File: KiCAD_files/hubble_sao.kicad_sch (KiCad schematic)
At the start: 41 parts, among them J1 Conn_02x03_Counter_Clockwise, J2 Conn_02x03_Odd_Even, Q1 DMP3099L-7, SW1 SW_Push_Shielded, U1 VEML3328, U2 LSM6DSO, U3 ATmega328PB-A, U4 TLV9062xD, U5 TLV9062xD

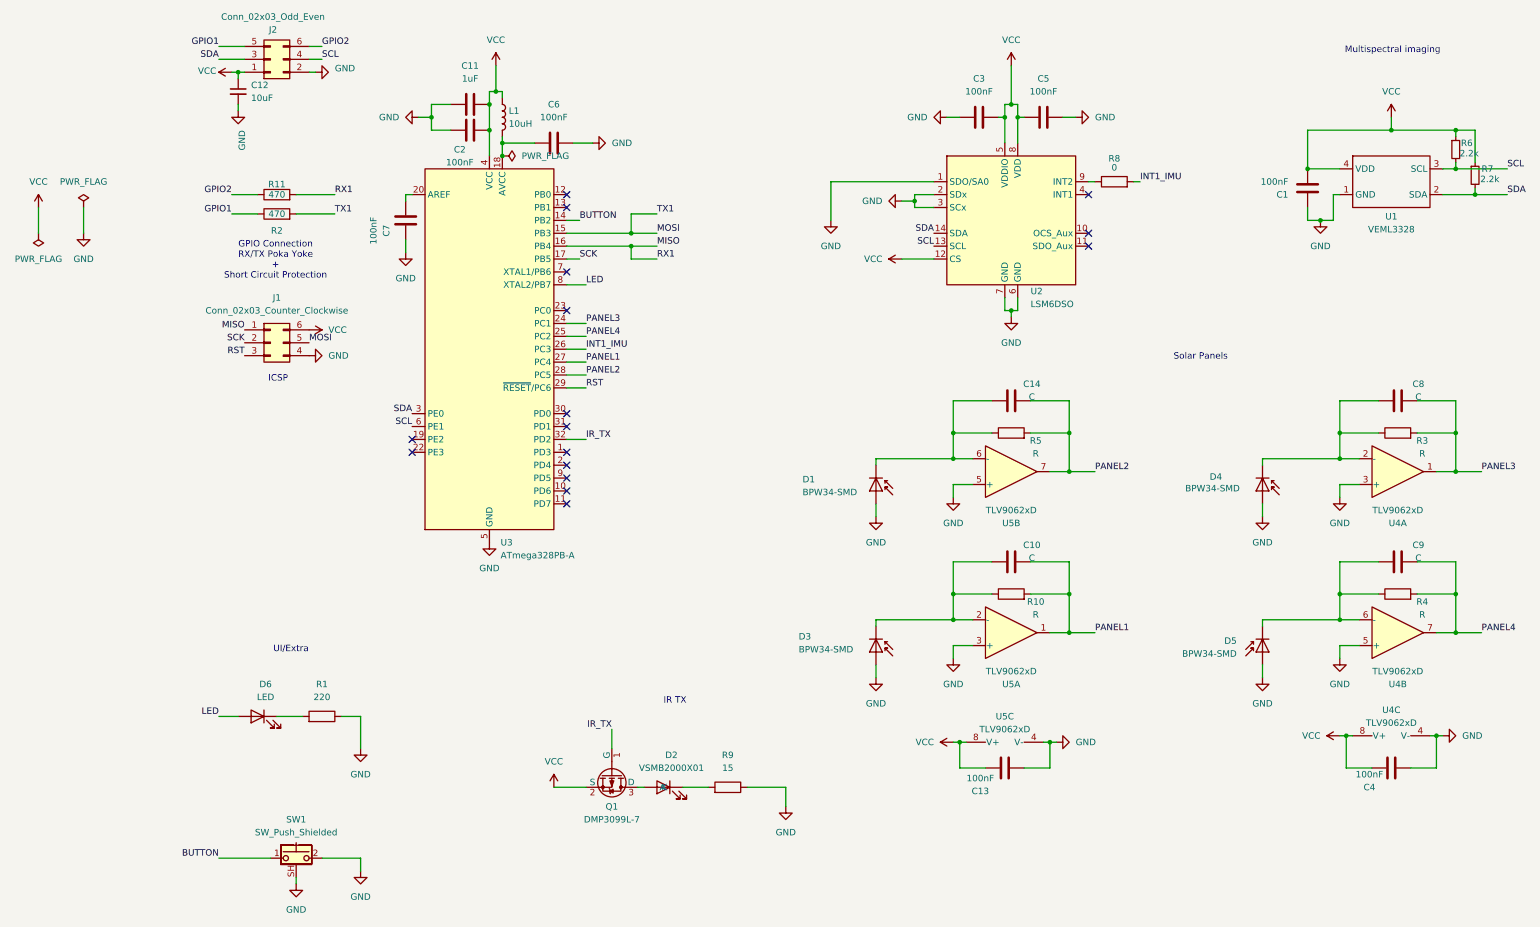
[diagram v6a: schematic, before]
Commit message: Modified RESET circuitry
- Added a switch to multiplex RESET and SCL on the pin header
- Added short-circuit protection on the RESET pin
- Added missing pullup resistor on the RESET pin. Before, RESET
was left floating. No problem was noticed on the prototype.
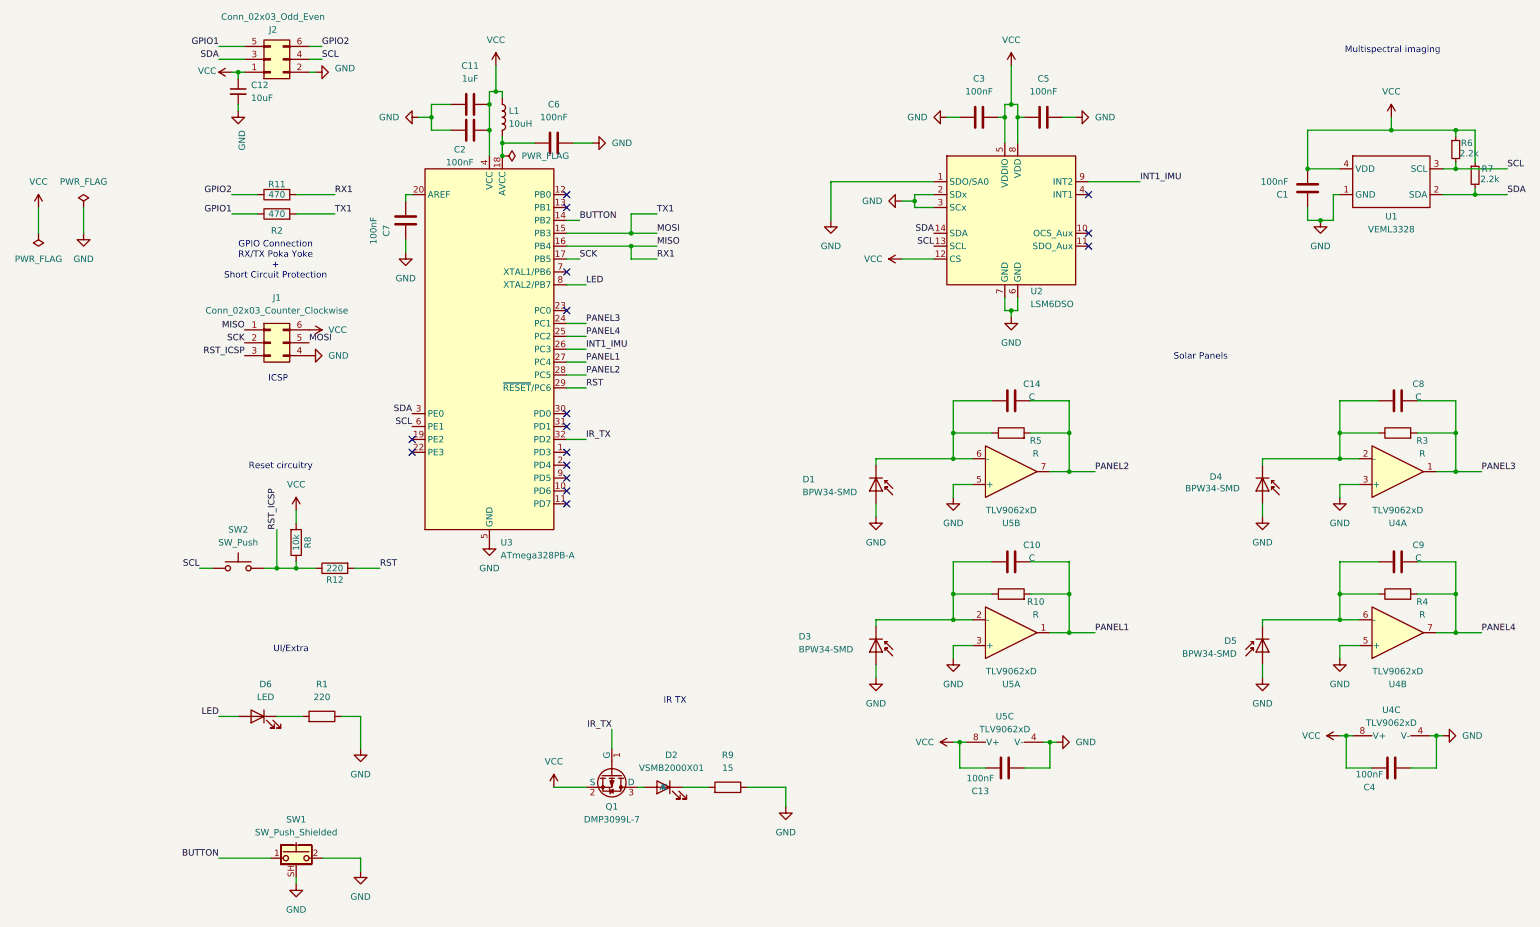
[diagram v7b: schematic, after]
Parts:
- added R12: 220, Resistor_SMD:R_0805_2012Metric_Pad1.20x1.40mm_HandSolder, symbol Device:R
- added SW2: SW_Push, Button_Switch_SMD:SW_SPST_B3U-1000P, symbol Switch:SW_Push
- R8: value 0 -> 10k
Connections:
- net INT1_IMU: now also U2.9 (INT2); no longer R8.2
- net RST: now also R12.2; no longer J1.3 (Pin_3)
- net SCL: now also SW2.1
- net VCC: now also R8.2
- net RST_ICSP: now reaches R8.1
- net RST_ICSP: now also J1.3 (Pin_3), R12.1, SW2.2; no longer U2.9 (INT2)
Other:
- note added: "Reset circuitry"

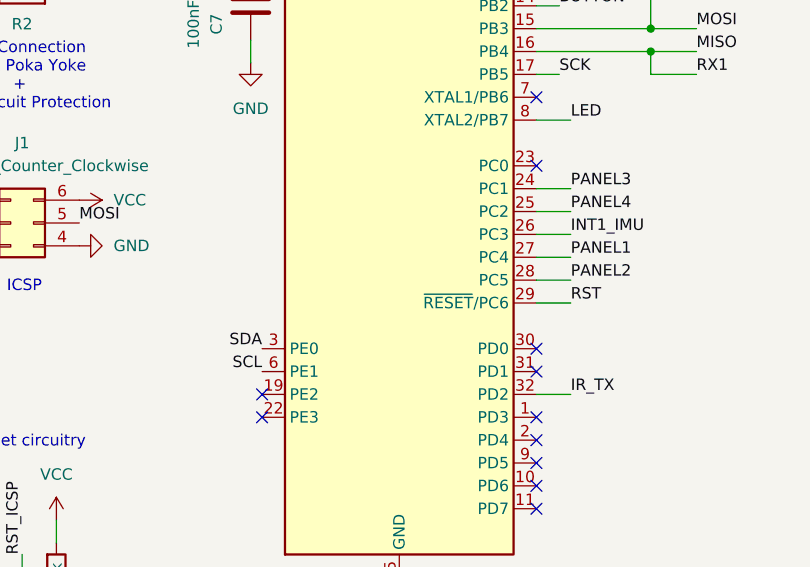
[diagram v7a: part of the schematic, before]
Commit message: Moved Panel3 to 19/PE2/ADC6/ICP3
This should enable the use of the Input Capture Pin 3.
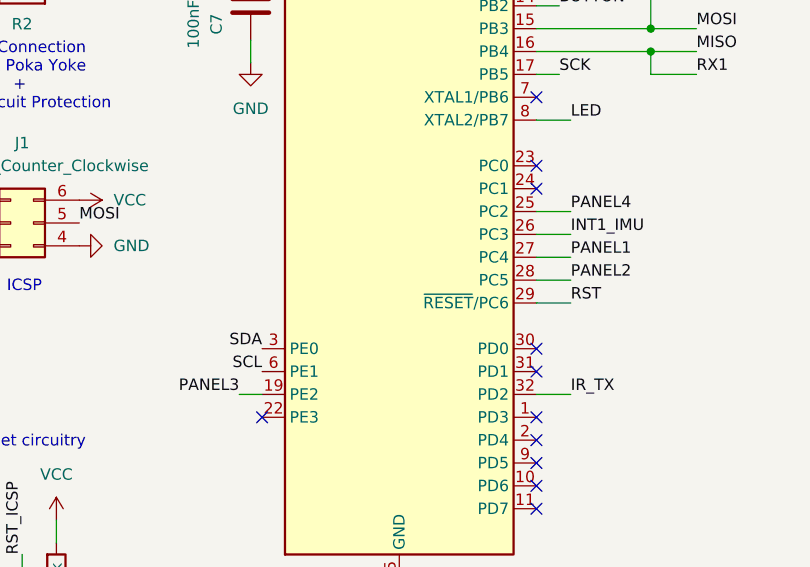
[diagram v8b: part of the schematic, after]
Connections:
- net PANEL3: now also U3.19 (PE2); no longer U3.24 (PC1)
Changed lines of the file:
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@@
-	)
-	(no_connect
-		(at 60.96 96.52)
 	)
 	(no_connect
@@
 	)
 	(no_connect
+		(at 91.44 73.66)
+	)
+	(no_connect
 		(at 91.44 91.44)
 	)
@@
 	(wire
 		(pts
-			(xy 91.44 73.66) (xy 95.25 73.66)
-		)
-		(stroke
-			(width 0)
-			(type default)
-		)
-	)
-	(wire
-		(pts
 			(xy 259.08 120.65) (xy 266.7 120.65)
 		)
@@
 		(pts
 			(xy 243.84 120.65) (xy 251.46 120.65)
+		)
+		(stroke
+			(width 0)
+			(type default)
+		)
+	)
+	(wire
+		(pts
+			(xy 58.42 96.52) (xy 60.96 96.52)
 		)
 		(stroke
@@
 	)
 	(label "PANEL3"
-		(at 95.25 73.66 0)
+		(at 58.42 96.52 180)
 		(fields_autoplaced yes)
 		(effects
@@
 				(size 1.27 1.27)
 			)
-			(justify left bottom)
-		)
-	)
+			(justify right bottom)
+		)
+	)
